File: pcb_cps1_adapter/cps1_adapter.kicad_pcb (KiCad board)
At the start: 2 copper layers, 70.1 x 63.5 mm, 28 parts, among them J1 Conn_02x05_Counter_Clockwise, J2 Conn_02x05_Counter_Clockwise, J3 Conn_02x05_Counter_Clockwise, J4 Conn_02x05_Counter_Clockwise, J5 Conn_02x05_Counter_Clockwise, U1 74LVC112, U2 WM8782

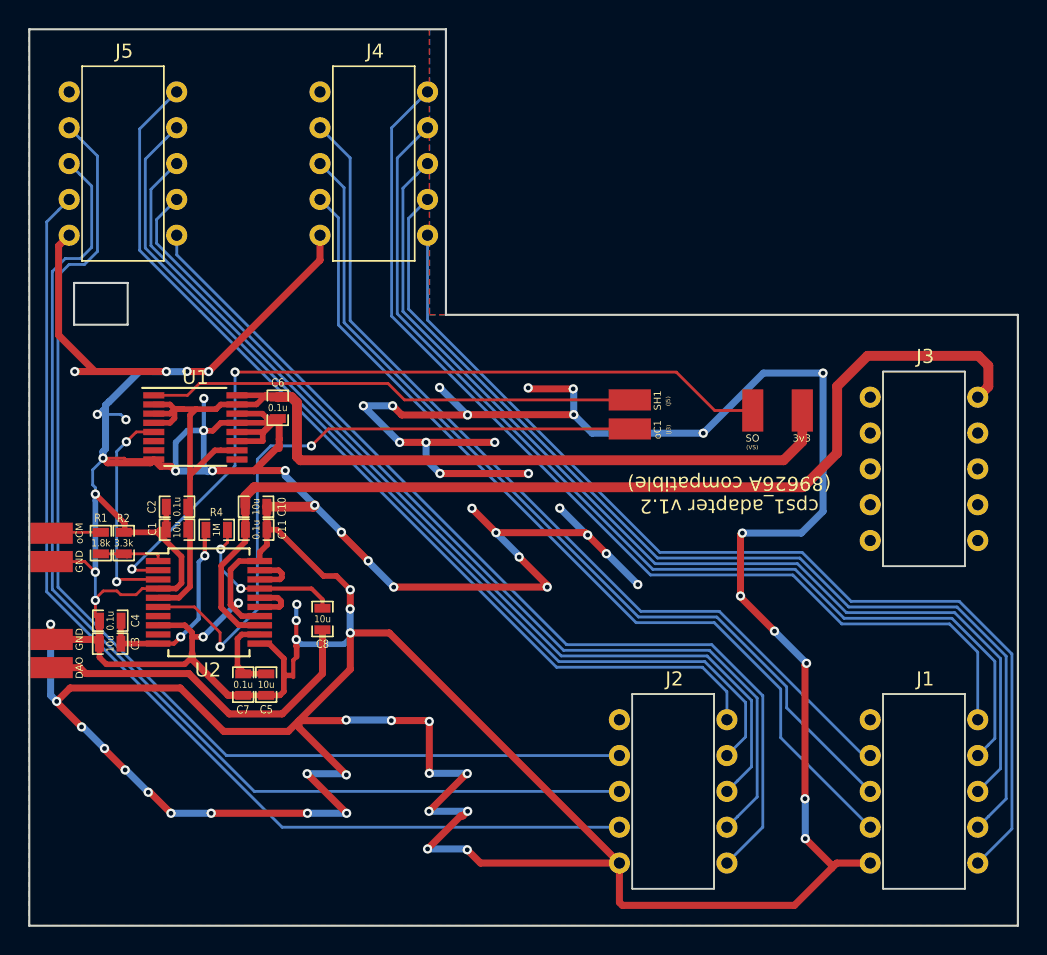
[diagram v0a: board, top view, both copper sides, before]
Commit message: update CPS1 adapter with CPS 1.5 Multi support
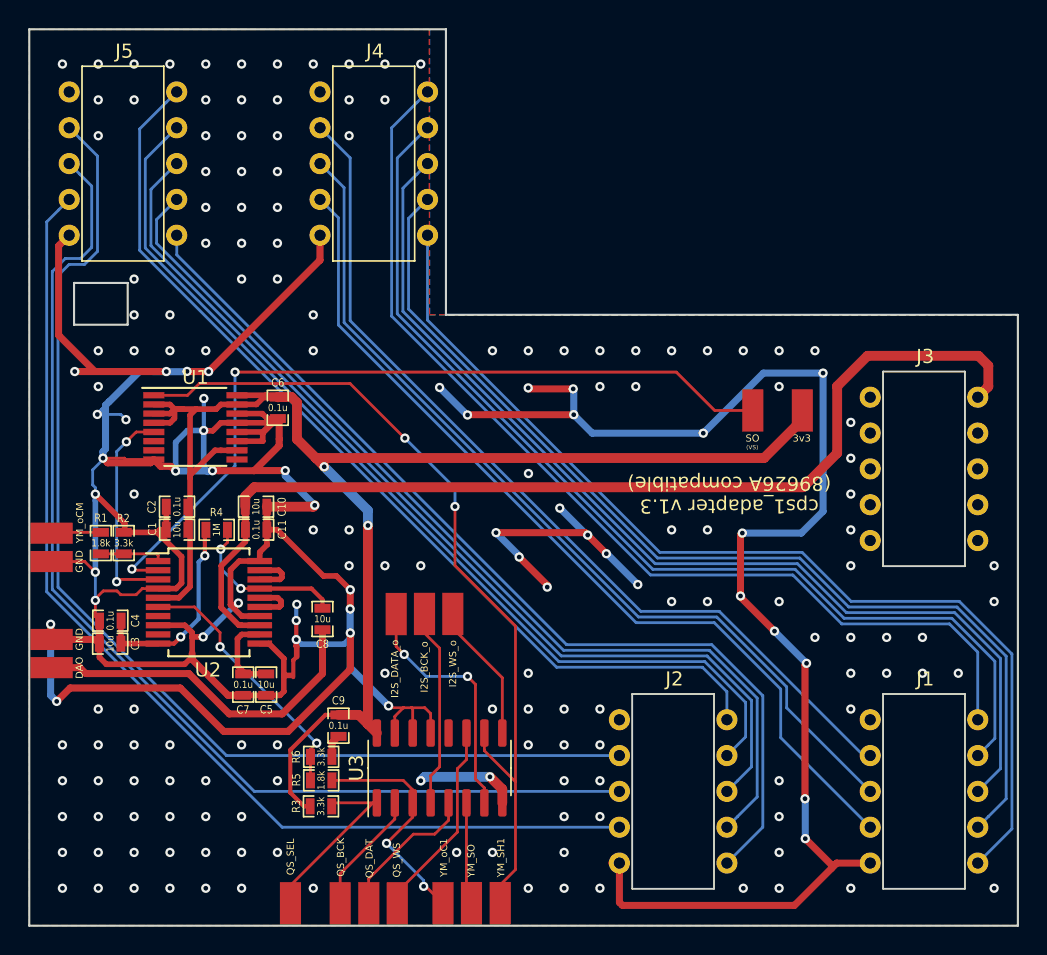
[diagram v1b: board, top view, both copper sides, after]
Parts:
- added C9: 0.1u, custom_components:SM0603_Capa_libcms, F.Cu at (62.5, 80.4)
- added R3: 3.3k, custom_components:SM0603_Resistor_libcms, F.Cu at (61.3, 86.1)
- added R5: 1.8k, custom_components:SM0603_Resistor_libcms, F.Cu at (61.3, 84.3)
- added R6: 3.3k, custom_components:SM0603_Resistor_libcms, F.Cu at (61.3, 82.6)
- added TP10: I2S_BCK_o, custom_components:SMD_PAD, F.Cu at (68.6, 72.5)
- added TP11: I2S_DATA_o, custom_components:SMD_PAD, F.Cu at (66.6, 72.5)
- added TP12: I2S_WS_o, custom_components:SMD_PAD, F.Cu at (70.6, 72.5)
- added TP13: QS_BCK, custom_components:SMD_PAD, F.Cu at (62.6, 93.0)
- added TP14: QS_DAT, custom_components:SMD_PAD, F.Cu at (64.7, 93.0)
- added TP15: QS_WS, custom_components:SMD_PAD, F.Cu at (66.7, 93.0)
- added TP16: QS_SEL, custom_components:SMD_PAD, F.Cu at (59.1, 93.0)
- added TP5: YM_SO, custom_components:SMD_PAD, F.Cu at (72.0, 93.0)
- added U3: 74LVC157, Package_SO:SOIC-16_3.9x9.9mm_P1.27mm, F.Cu at (69.7, 83.4)
- TP6: value oC1 -> YM_oC1
- TP7: value SH1 -> YM_SH1
- TP9: value oCM -> YM_oCM
- moved TP7 36.8 mm to (74.0, 93.0), turned to 90 degrees
- moved TP6 36.1 mm to (69.9, 93.0), turned to 90 degrees
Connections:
- net /SH1 renamed /YM_SH1
- net /oCM renamed /YM_oCM
- J1 pad 1: Net-(J1-Pad1) -> unconnected-(J1-Pad1)
- J2 pad 1: Net-(J2-Pad1) -> unconnected-(J2-Pad1)
- J3 pad 1: Net-(J3-Pad1) -> unconnected-(J3-Pad1)
- J3 pad 2: Net-(J3-Pad2) -> unconnected-(J3-Pad2)
- J3 pad 3: Net-(J3-Pad3) -> unconnected-(J3-Pad3)
- J3 pad 4: Net-(J3-Pad4) -> unconnected-(J3-Pad4)
- J3 pad 5: Net-(J3-Pad5) -> unconnected-(J3-Pad5)
- J3 pad 6: Net-(J3-Pad6) -> unconnected-(J3-Pad6)
- J3 pad 7: Net-(J3-Pad7) -> unconnected-(J3-Pad7)
- J3 pad 8: Net-(J3-Pad8) -> unconnected-(J3-Pad8)
- J3 pad 9: Net-(J3-Pad9) -> unconnected-(J3-Pad9)
- J4 pad 1: Net-(J4-Pad1) -> unconnected-(J4-Pad1)
- J5 pad 1: Net-(J5-Pad1) -> unconnected-(J5-Pad1)
- TP6 pad 1: /oC1 -> /YM_oC1
- U1 pad 6: Net-(U1-Pad6) -> unconnected-(U1-Pad6)
- U1 pad 7: Net-(U1-Pad7) -> unconnected-(U1-Pad7)
- U1 pad 9: Net-(U1-Pad9) -> unconnected-(U1-Pad9)
- U2 pad 6: /oC1 -> Net-(R5-Pad2)
- U2 pad 7: Net-(U2-Pad7) -> unconnected-(U2-Pad7)
- U2 pad 9: Net-(U2-Pad9) -> unconnected-(U2-Pad9)
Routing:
- net GND: track 507.4 -> 380.7 mm, vias 76 -> 194
- net /oC1: track 47.8 -> 0.00 mm, vias 2 -> 0
- net /DVDD3V3: track 82.5 -> 115.4 mm, vias 0 -> 2
- net /YM_SH1: track 34.6 -> 60.8 mm, vias 0 -> 2
- net Net-(R5-Pad2): track 0.00 -> 18.7 mm, vias 0 -> 2
- net Net-(TP11-Pad1): track 0.00 -> 17.7 mm, vias 0 -> 2
- net /YM_oC1: track 0.00 -> 16.6 mm, vias 0 -> 2
- net Net-(TP10-Pad1): track 0.00 -> 14.1 mm
- net /QS_WS: track 0.00 -> 14.1 mm
- net Net-(R3-Pad1): track 0.00 -> 13.1 mm
- net /QS_DAT: track 0.00 -> 10.3 mm
- net Net-(TP12-Pad1): track 0.00 -> 9.90 mm
- net /QS_BCK: track 0.00 -> 8.72 mm
- net /YM_SO: track 0.00 -> 7.30 mm
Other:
- net class Default removed
- net class Power removed
- board text added: "cps1_adapter v1.3 (89626A compatible)"
- board text removed: "(J3)"
- board text removed: "(J5)"
- board text removed: "cps1_adapter v1.2 (89626A compatible)"
